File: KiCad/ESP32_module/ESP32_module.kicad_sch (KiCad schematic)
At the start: 20 parts, among them J1 Conn_01x05_Pin, J2 Conn_01x05_Pin, J3 Conn_01x05_Pin, J4 Conn_01x05_Pin, J5 Conn_01x02_Pin, J6 Conn_01x02_Pin, J7 Conn_01x02_Pin, J8 Conn_01x02_Pin, J9 Conn_01x02_Pin

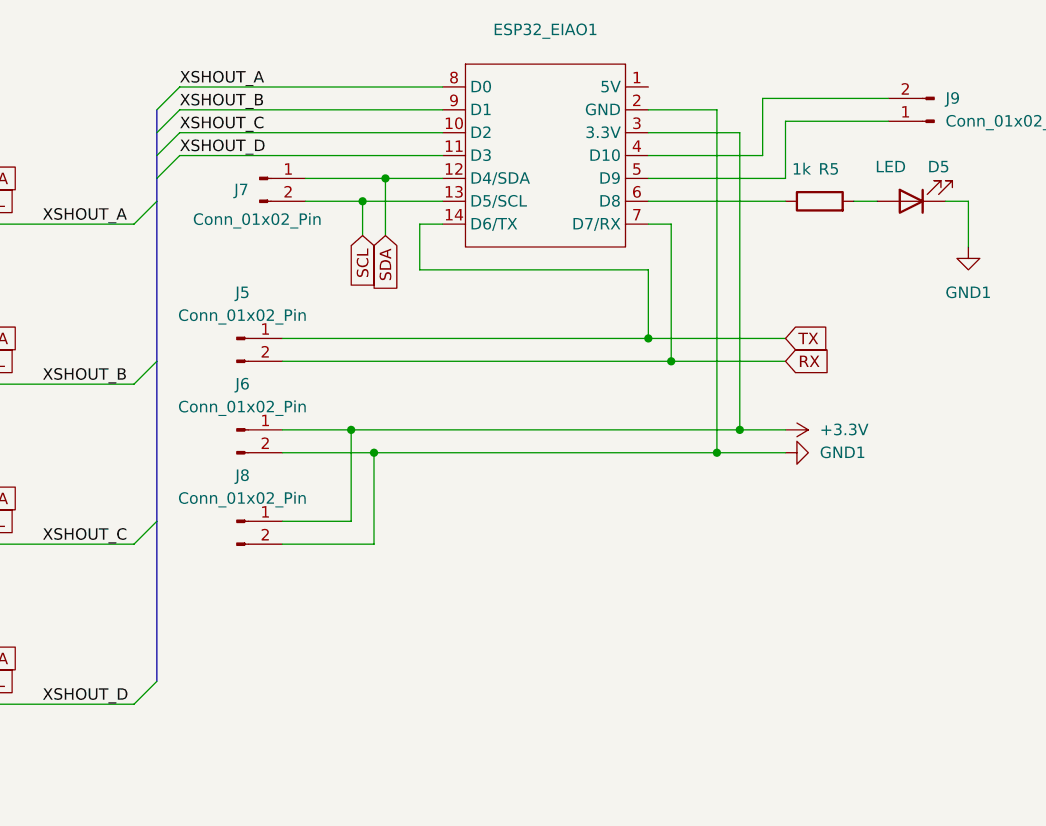
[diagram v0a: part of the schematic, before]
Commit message: add I2C pullup resister
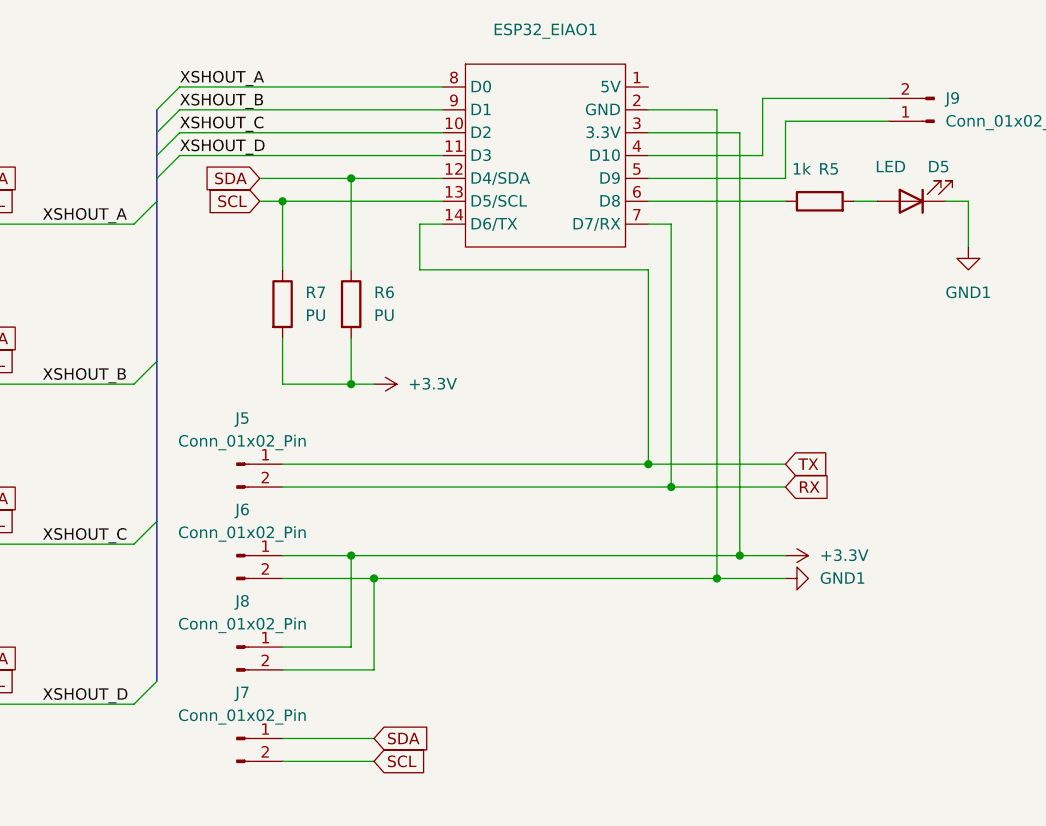
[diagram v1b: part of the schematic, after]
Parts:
- added R6, R7: PU, symbol Device:R
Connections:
- net +3.3V: now also R6.2, R7.2
- net SCL: now also R7.1
- net SDA: now also R6.1
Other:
- moved on the sheet: J5, J6, J8

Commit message: add fet
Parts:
- removed J9: Conn_01x02_Pin, symbol Connector:Conn_01x02_Pin
- added D6, D7, D8, D9: LED, symbol Device:LED
- added FET1: ~, symbol esp32_lib:μPA2753GR
- added R12, R13, R14, R15: 1k, symbol Device:R
- added R4, R5: 400, symbol Device:R
- added R6, R7: 10k, symbol Device:R
- R10: renamed from R3; value 1k -> 10
- R11: renamed from R4; value 1k -> 10
- R8: renamed from R1; value 1k -> 10
- R9: renamed from R2; value 1k -> 10
- renumbered D5 to D1, D1 to D2, D2 to D3, D3 to D4, D4 to D5, J8 to J7, J7 to J8, R7 to R1, R6 to R2, R5 to R3
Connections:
- net +3.3V: now also FET1.1 (Source_1), FET1.3 (Source_2), R6.2, R7.2; no longer R10.1, R11.1, R8.1, R9.1
- net GND1: now also D6.1 (K), D7.1 (K), D8.1 (K), D9.1 (K)
- net at ESP32_EIAO1.5 (D9): now also R5.1
- net at ESP32_EIAO1.4 (D10): now also R4.1
- new net: FET1.5 (Drain_2), FET1.6 (Drain_2), R10.1, R11.1, R8.1, R9.1
- new net: D8.2 (A), R14.2
- new net: FET1.7 (Drain_1), FET1.8 (Drain_1), R12.1, R13.1, R14.1, R15.1
- new net: FET1.4 (Gate_2), R5.2, R7.1
- new net: D9.2 (A), R15.2
- new net: D7.2 (A), R13.2
- new net: FET1.2 (Gate_1), R4.2, R6.1
- new net: D6.2 (A), R12.2
- no-connect marks 0 -> 1
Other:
- moved on the sheet: D1, D2, D3, D4, D5, ESP32_EIAO1, J1, J2, J3, J4, J5, J6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

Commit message: add PCB design
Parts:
- removed ESP32_EIAO1: ~, symbol esp32_lib:xiao_esp32
- added J9: Conn_01x02_Pin, esp32_lib_pcb:2.54mm_pin, symbol Connector:Conn_01x02_Pin
- added M1: ESP32_XAIO, esp32_lib_pcb:ESP32_XIAO, symbol esp32_lib:xiao_esp32
- D1, D6, D7, D8, D9: footprint (none) -> Diode_SMD:D_0603_1608Metric_Pad1.05x0.95mm_HandSolder
- D2, D3, D4, D5: footprint (none) -> esp32_lib_pcb:LEDM3528X190N
- FET1: value ~ -> μPA2753GR; footprint (none) -> Package_SO:HSOP-8-1EP_3.9x4.9mm_P1.27mm_EP2.3x2.3mm
- J1, J2, J3, J4: footprint (none) -> Connector_JST:JST_PH_S5B-PH-K_1x05_P2.00mm_Horizontal
- J5, J6: footprint (none) -> Connector_JST:JST_PH_S2B-PH-K_1x02_P2.00mm_Horizontal
- J7, J8: footprint (none) -> esp32_lib_pcb:2.54mm_pin
- R1, R10, R11, R12, R13, R14, R15, R2, R3, R4, R5, R6, R7, R8, R9: footprint (none) -> Resistor_SMD:R_0603_1608Metric
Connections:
- net +3.3V: now also M1.3 (3.3V)
- net GND1: now also M1.2 (GND)
- net RX: now also J9.2 (Pin_2), M1.7 (D7/RX)
- net SCL: now also M1.13 (D5/SCL)
- net SDA: now also M1.12 (D4/SDA)
- net TX: now also J9.1 (Pin_1), M1.14 (D6/TX)
- net XSHOUT_A: now also M1.8 (D0)
- net XSHOUT_B: now also M1.9 (D1)
- net XSHOUT_C: now also M1.10 (D2)
- net XSHOUT_D: now also M1.11 (D3)
- net at R5.1: now also M1.5 (D9)
- net at R4.1: now also M1.4 (D10)
- net at R3.1: now also M1.6 (D8)
